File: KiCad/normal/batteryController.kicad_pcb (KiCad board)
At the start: 2 copper layers, 44 x 18 mm, 11 parts, among them J1 Conn_02x08_Counter_Clockwise, J2 Screw_Terminal_01x02, J3 USB_A, U1 ATtiny45V-10P, U2 L7806CV, U3 L78L05_SOT89

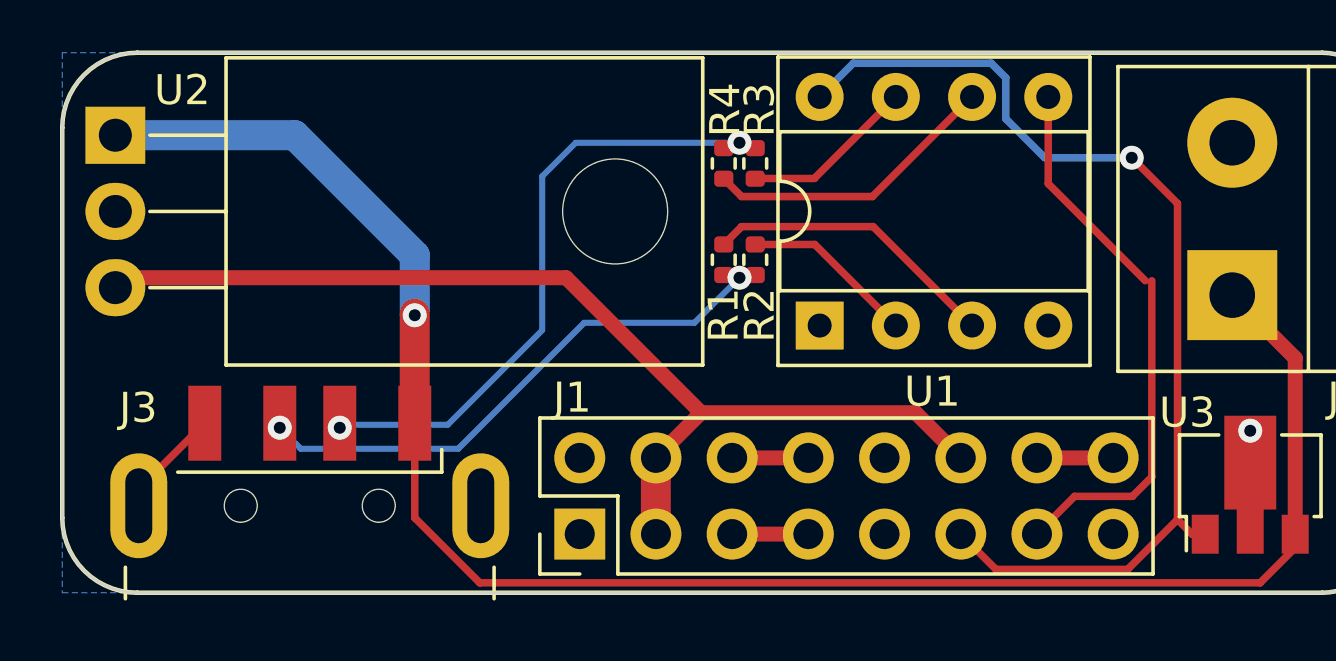
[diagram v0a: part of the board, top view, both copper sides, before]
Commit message: added panelization
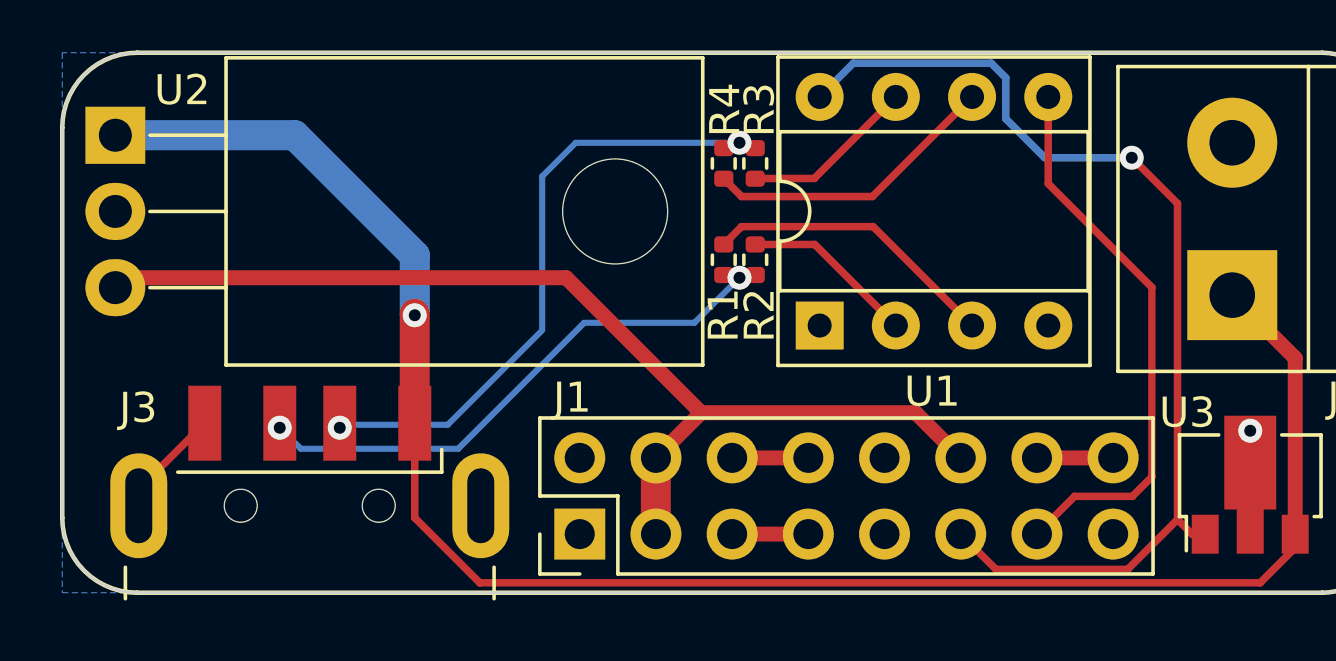
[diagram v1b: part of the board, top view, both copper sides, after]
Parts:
- moved J3 5.90 mm to (181.2, 116.1)
- moved G*** 0.56 mm to (213.2, 115.0)
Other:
- board text added: "github.com/algnor/qc3-bc"

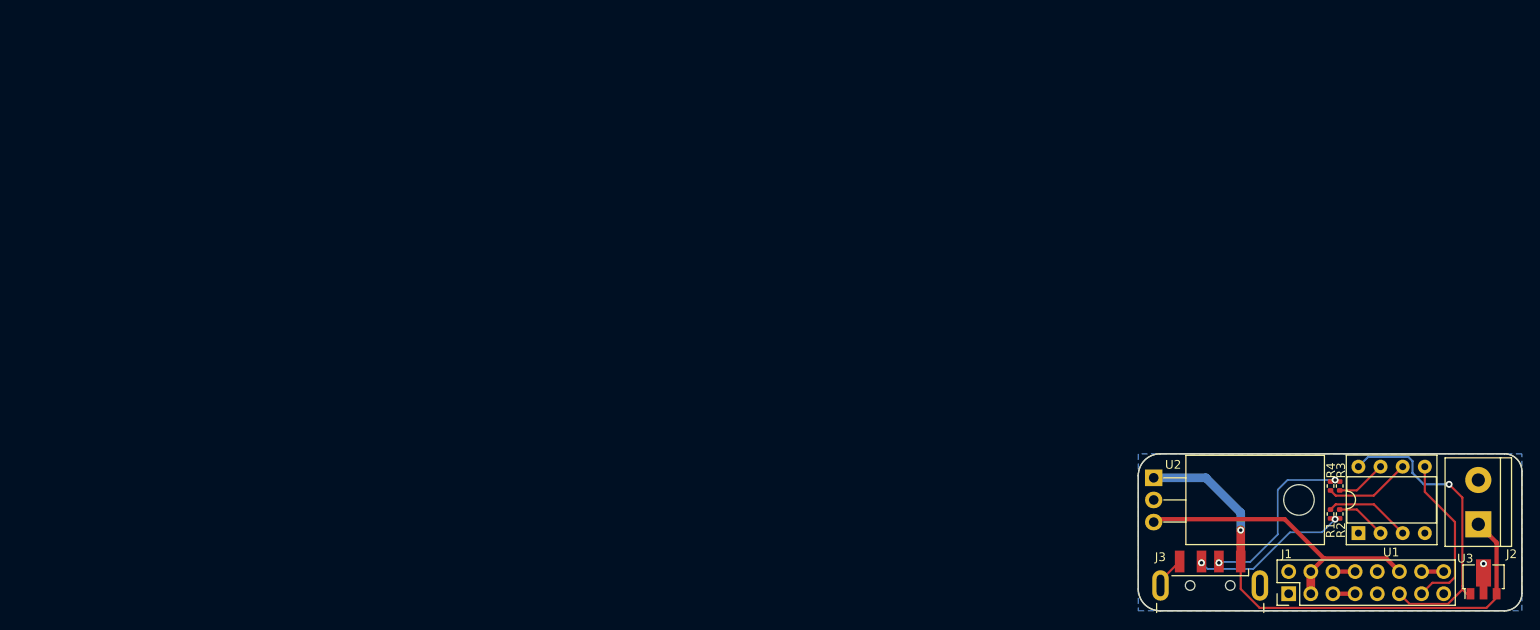
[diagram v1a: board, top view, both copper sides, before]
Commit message: redesign to use switching voltage regulator
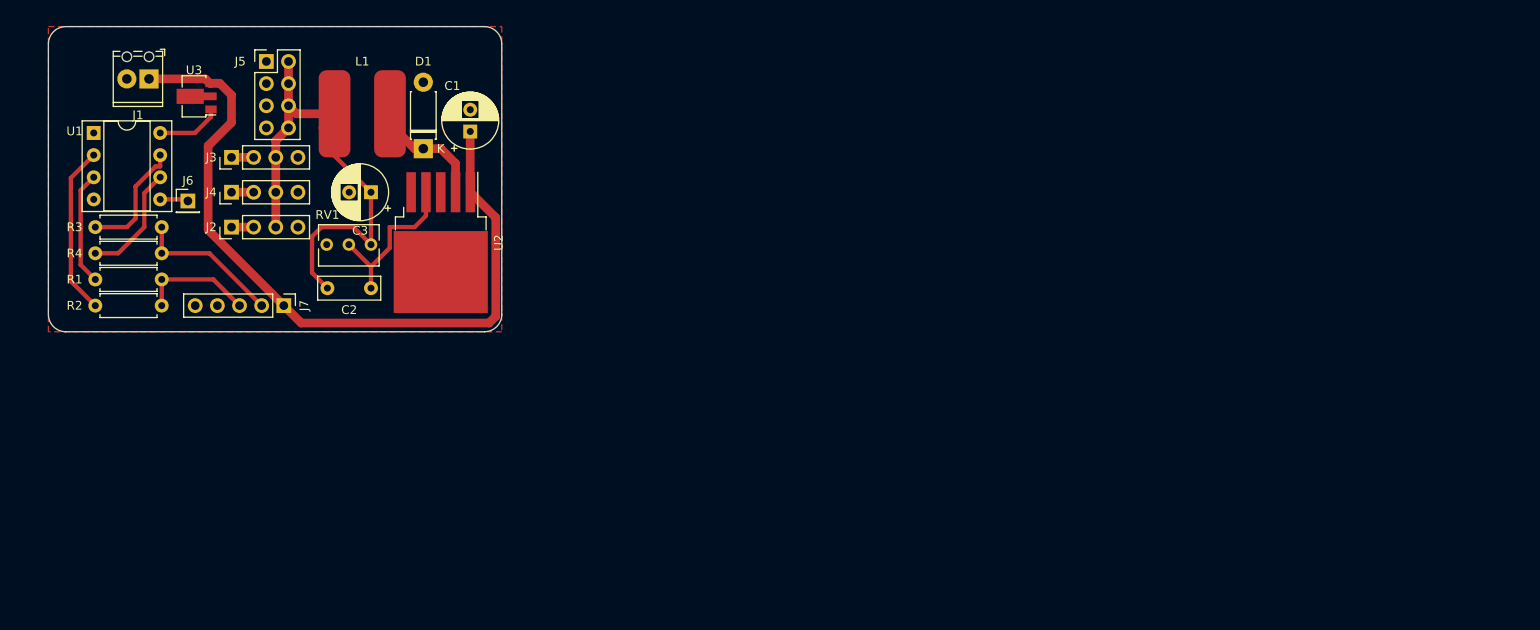
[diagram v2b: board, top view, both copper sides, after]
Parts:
- removed G***: LOGO, personal-icons:ABB-gym-logo-4mm
- added C1: 100uF, Capacitor_THT:CP_Radial_D6.3mm_P2.50mm, F.Cu at (96.4, 63.0)
- added C2: 15nF, Capacitor_THT:C_Rect_L7.0mm_W2.5mm_P5.00mm, F.Cu at (85.0, 81.0)
- added C3: 100uF, Capacitor_THT:CP_Radial_D6.3mm_P2.50mm, F.Cu at (85.0, 70.0)
- added D1: D_Schottky, Diode_THT:D_DO-41_SOD81_P7.62mm_Horizontal, F.Cu at (91.0, 65.0)
- added J4: Conn_01x04_Male, Connector_PinHeader_2.54mm:PinHeader_1x04_P2.54mm_Vertical, F.Cu at (69.0, 70.0)
- added J5: Conn_02x04_Odd_Even, Connector_PinHeader_2.54mm:PinHeader_2x04_P2.54mm_Vertical, F.Cu at (73.0, 55.0)
- added J6: Conn_01x01_Male, Connector_PinHeader_2.54mm:PinHeader_1x01_P2.54mm_Vertical, F.Cu at (64.0, 71.0)
- added J7: USB_A, Connector_PinHeader_2.54mm:PinHeader_1x05_P2.54mm_Vertical, F.Cu at (75.0, 83.0)
- added L1: 22uH, custom:sdr1006, F.Cu at (84.0, 61.0)
- added RV1: 10k, Potentiometer_THT:Potentiometer_Bourns_3266Y_Vertical, F.Cu at (85.0, 76.0)
- J1: value Conn_02x08_Counter_Clockwise -> Screw_Terminal_01x02; footprint Connector_PinHeader_2.54mm:PinHeader_2x08_P2.54mm_Vertical -> TerminalBlock_Phoenix:TerminalBlock_Phoenix_MPT-0,5-2-2.54_1x02_P2.54mm_Horizontal
- J2: value Screw_Terminal_01x02 -> Conn_01x04_Male; footprint TerminalBlock:TerminalBlock_bornier-2_P5.08mm -> Connector_PinHeader_2.54mm:PinHeader_1x04_P2.54mm_Vertical
- J3: value USB_A -> Conn_01x04_Male; footprint Connector_USB:USB_A_CNCTech_1001-011-01101_Horizontal -> Connector_PinHeader_2.54mm:PinHeader_1x04_P2.54mm_Vertical
- R1, R2, R3, R4: footprint Resistor_SMD:R_0402_1005Metric -> Resistor_THT:R_Axial_DIN0207_L6.3mm_D2.5mm_P7.62mm_Horizontal
- U2: value L7806CV -> LM2596S-ADJ; footprint Package_TO_SOT_THT:TO-220-3_Horizontal_TabDown -> Package_TO_SOT_SMD:TO-263-5_TabPin3
- moved U3 157.7 mm to (65.0, 59.0), turned to 180 degrees
- moved U1 152.1 mm to (53.2, 63.2), turned to 0 degrees
- moved J2 147.0 mm to (69.0, 74.0)
- moved R3 145.8 mm to (53.4, 74.0), turned to 0 degrees
- moved R2 144.7 mm to (53.4, 83.0), turned to 0 degrees
- moved R1 144.2 mm to (53.4, 80.0), turned to 0 degrees
- moved R4 144.2 mm to (53.4, 77.0), turned to 0 degrees
- moved J1 143.4 mm to (59.5, 57.0), turned to 180 degrees
- moved J3 122.9 mm to (69.0, 66.0), turned to 90 degrees
- moved U2 86.1 mm to (93.0, 75.8)
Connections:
- J1 pad 1: /GND -> /VBUS
- J1 pad 2: /GND -> GND
- J2 pad 1: /VBUS -> Net-(J2-Pad1)
- J2 pad 2: /GND -> Net-(J2-Pad1)
- J3 pad 1: /VBUS -> Net-(J3-Pad1)
- J3 pad 2: /D- -> Net-(J3-Pad1)
- J3 pad 3: /D+ -> /OUT
- J3 pad 4: /GND -> GND
- U1 pad 4: /GND -> GND
- U2 pad 2: /GND -> /ROUT
- U2 pad 3: /6V -> GND
- U3 pad 2: /GND -> GND
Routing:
- net /OUT: track 0.00 -> 62.8 mm
- net /6V: track 35.5 -> 0.00 mm
- net /5V: track 35.2 -> 7.45 mm, vias 1 -> 0
- net /VBUS: track 60.7 -> 86.8 mm, vias 1 -> 0
- net /FB: track 0.00 -> 20.7 mm
- net /controll pin: track 18.7 -> 3.51 mm
- net /ROUT: track 0.00 -> 14.7 mm
- net Net-(R2-Pad1): track 6.21 -> 19.5 mm
- net Net-(R3-Pad1): track 5.81 -> 13.8 mm
- net /D+: track 19.6 -> 13.2 mm, vias 2 -> 0
- net /D-: track 21.3 -> 16.9 mm, vias 2 -> 0
- net /GND: track 3.66 -> 0.00 mm, vias 1 -> 0
- net Net-(R4-Pad1): track 9.90 -> 13.3 mm
- net Net-(R1-Pad1): track 9.89 -> 13.0 mm
- net Net-(J1-Pad6): track 2.54 -> 0.00 mm
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- added copper zone on F.Cu, net GND
- removed copper zone on B.Cu, net /GND
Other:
- board size 44 x 18 mm -> 52 x 35 mm
- board text removed: "3mm"
- board text removed: "3x"
- board text removed: "5V"
- board text removed: "6V"
- board text removed: "D"
- board text removed: "Designed by Algot"
- board text removed: "G"
- board text removed: "PWM"
- board text removed: "github.com/algnor/qc3-bc"

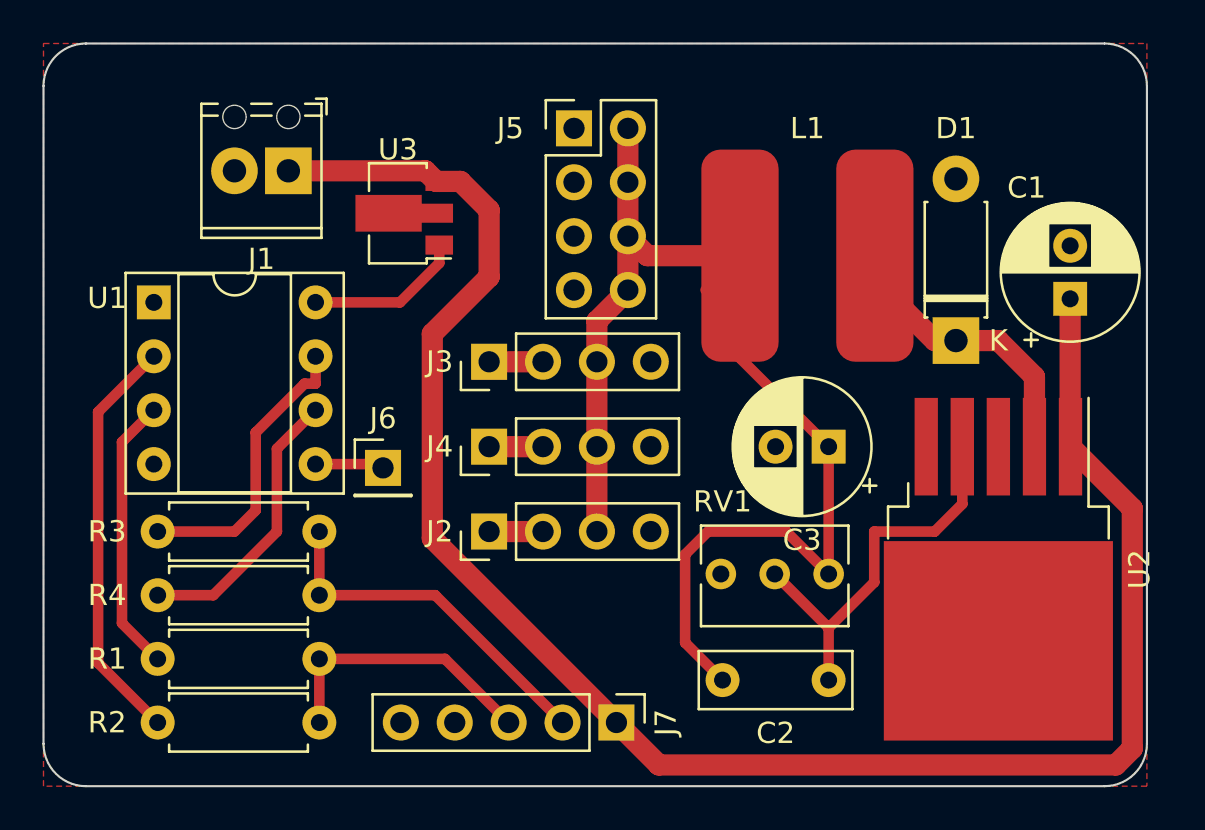
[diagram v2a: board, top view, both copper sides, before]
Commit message: changed 5v regulator
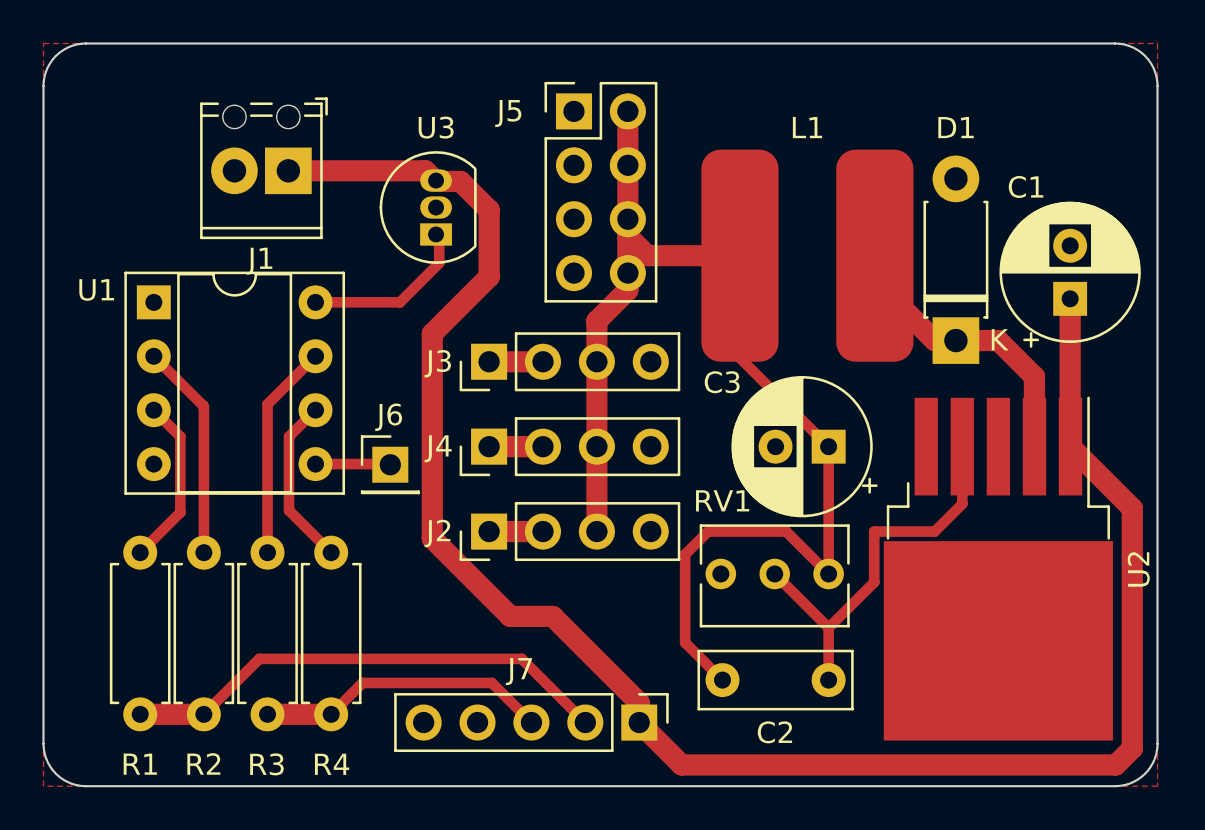
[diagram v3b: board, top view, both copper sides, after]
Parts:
- U3: value L78L05_SOT89 -> LP2950-3.3_TO92; footprint Package_TO_SOT_SMD:SOT-89-3 -> Package_TO_SOT_THT:TO-92_Inline
- moved R4 8.42 mm to (61.6, 75.0), turned to -90 degrees
- moved R2 8.30 mm to (55.6, 75.0), turned to -90 degrees
- moved R3 5.27 mm to (58.6, 75.0), turned to -90 degrees
- moved R1 5.07 mm to (52.6, 75.0), turned to -90 degrees
- moved U3 1.80 mm to (66.5, 60.0), turned to 90 degrees
- moved J7 1.08 mm to (76.1, 83.0)
- moved J5 0.80 mm to (73.0, 54.2)
- moved J6 0.37 mm to (64.3, 70.9)
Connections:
- J7 pad 2: /D- -> Net-(R1-Pad2)
- J7 pad 3: /D+ -> Net-(J7-Pad3)
- R1 pad 2: /D+ -> Net-(R1-Pad2)
- R2 pad 2: /D+ -> Net-(R1-Pad2)
- R3 pad 2: /D- -> Net-(J7-Pad3)
- R4 pad 2: /D- -> Net-(J7-Pad3)
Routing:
- net Net-(R1-Pad2): track 0.00 -> 23.3 mm
- net /D-: track 16.9 -> 0.00 mm
- net Net-(J7-Pad3): track 0.00 -> 13.8 mm
- net /D+: track 13.2 -> 0.00 mm
- net Net-(R2-Pad1): track 19.5 -> 10.2 mm
- net /OUT: track 62.8 -> 56.7 mm
- net Net-(R4-Pad1): track 13.3 -> 8.06 mm
- net Net-(R1-Pad1): track 13.0 -> 8.02 mm
- net Net-(R3-Pad1): track 13.8 -> 10.2 mm
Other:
- board size 52 x 35 mm -> 52.5 x 35 mm

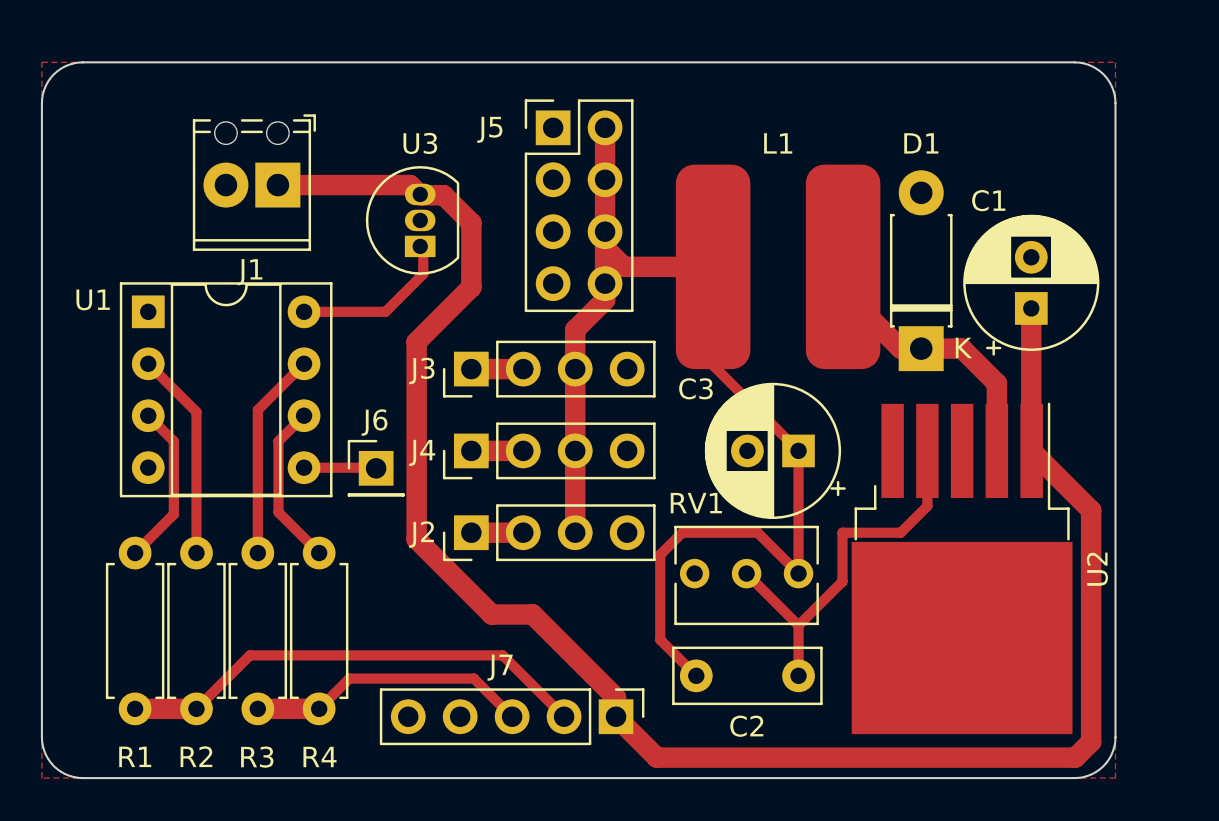
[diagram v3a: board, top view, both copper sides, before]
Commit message: spaced out more for pcb milling
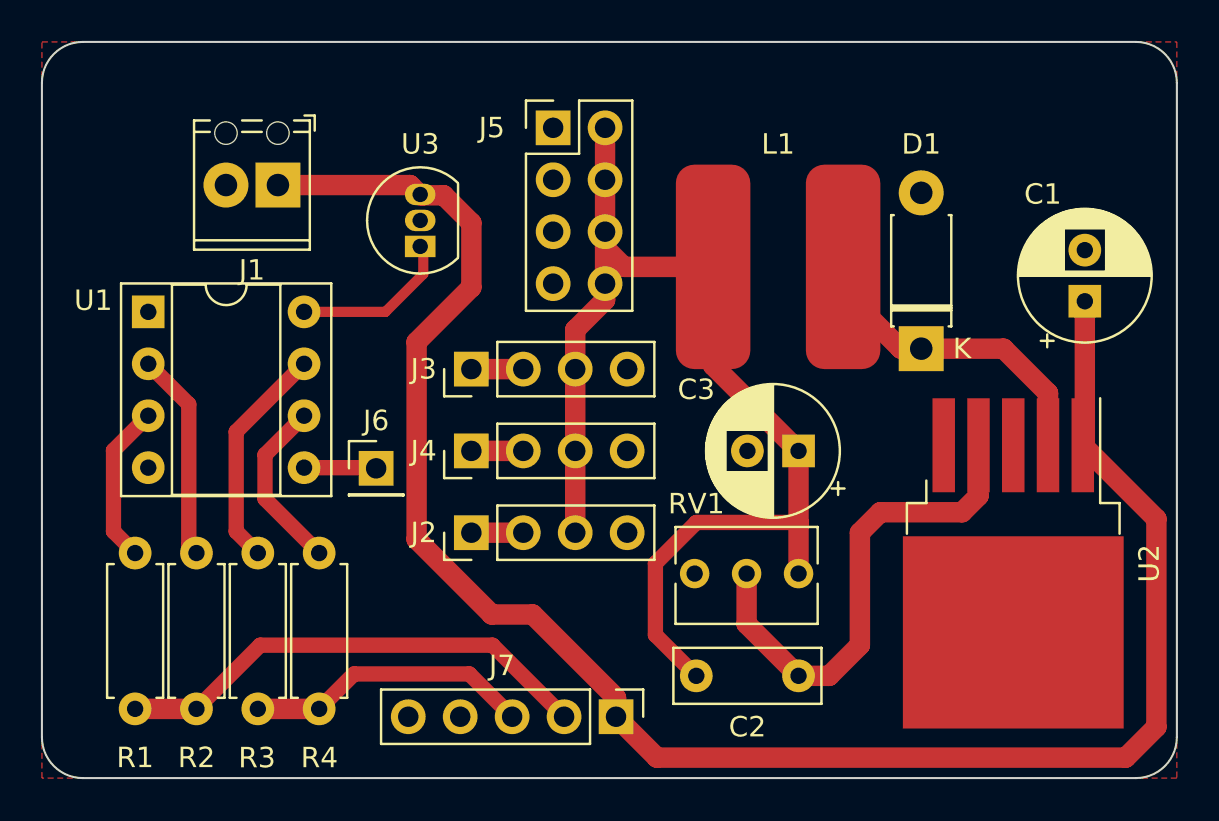
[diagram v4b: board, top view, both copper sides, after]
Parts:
- moved C1 2.64 mm to (99.0, 62.7)
- moved U2 2.52 mm to (95.5, 75.5)
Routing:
- net /VBUS: track 86.6 -> 90.9 mm
- net /FB: track 20.7 -> 24.2 mm
- net /ROUT: track 14.7 -> 17.5 mm
- net Net-(R3-Pad1): track 10.2 -> 11.1 mm
- net Net-(R4-Pad1): track 8.06 -> 8.60 mm
- net /OUT: track 56.7 -> 56.2 mm
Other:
- board size 52.5 x 35 mm -> 55.5 x 36 mm
